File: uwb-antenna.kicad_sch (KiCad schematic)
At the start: 59 parts, among them J1 USB C, J2 Battery, J4 Conn_ST_STDC14, SW1 ~{PB}, SW2 BOOT0, SW4 ~{SR}, U1 STM6600, U2 BQ24074RGT, U3 TPS63001, U5 STM32L432KBUx

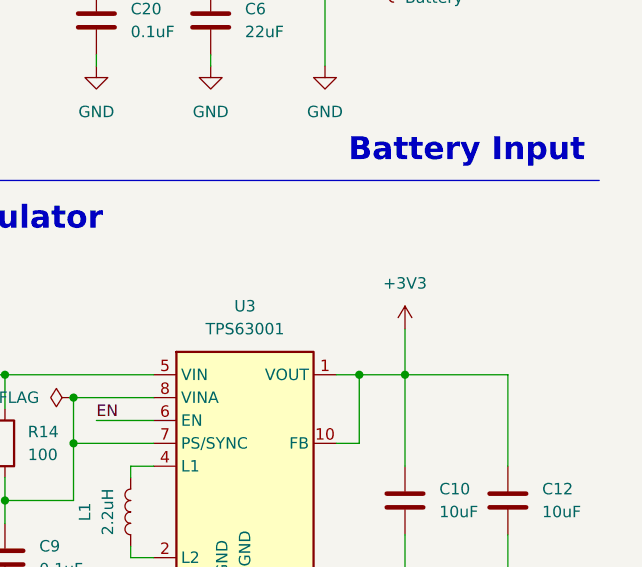
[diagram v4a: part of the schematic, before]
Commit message: add some traces
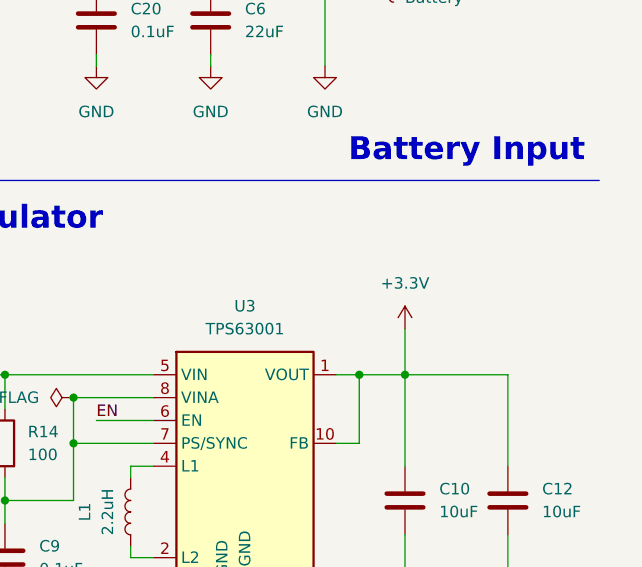
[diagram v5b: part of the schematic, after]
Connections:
- net +3V3 is gone; now on net +3.3V: C10.1, C12.1, U3.1 (VOUT), U3.10 (FB)
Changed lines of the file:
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@@
 	)
 	(symbol
-		(lib_id "power:+3V3")
-		(at 262.89 58.42 0)
-		(unit 1)
-		(exclude_from_sim no)
-		(in_bom yes)
-		(on_board yes)
-		(dnp no)
-		(fields_autoplaced yes)
-		(property "Reference" "#PWR033"
-			(at 262.89 62.23 0)
-			(effects
-				(font
-					(size 1.27 1.27)
-				)
-				(hide yes)
-			)
-		)
-		(property "Value" "+3V3"
-			(at 262.89 53.34 0)
-			(effects
-				(font
-					(size 1.27 1.27)
-				)
-			)
-		)
-		(property "Footprint" ""
-			(at 262.89 58.42 0)
-			(effects
-				(font
-					(size 1.27 1.27)
-				)
-				(hide yes)
-			)
-		)
-		(property "Datasheet" ""
-			(at 262.89 58.42 0)
-			(effects
-				(font
-					(size 1.27 1.27)
-				)
-				(hide yes)
-			)
-		)
-		(property "Description" "Power symbol creates a global label with name \"+3V3\""
-			(at 262.89 58.42 0)
-			(effects
-				(font
-					(size 1.27 1.27)
-				)
-				(hide yes)
-			)
-		)
-		(pin "1"
-		)
-		(instances
-			(project ""
-				(path "/f7e38ffb-df5d-4aea-a3f5-296732509798"
-					(reference "#PWR033")
-					(unit 1)
-				)
-			)
-		)
-	)
-	(symbol
 		(lib_id "Device:C")
 		(at 157.48 139.7 0)
@@
 					(unit 1)
 				)
+			)
+		)
+	)
+	(symbol
+		(lib_id "power:+3.3V")
+		(at 262.89 58.42 0)
+		(unit 1)
+		(exclude_from_sim no)
+		(in_bom yes)
+		(on_board yes)
+		(dnp no)
+		(fields_autoplaced yes)
+		(property "Reference" "#PWR033"
+			(at 262.89 62.23 0)
+			(effects
+				(font
+					(size 1.27 1.27)
+				)
+				(hide yes)
+			)
+		)
+		(property "Value" "+3.3V"
+			(at 262.89 53.34 0)
+			(effects
+				(font
+					(size 1.27 1.27)
+				)
+			)
+		)
+		(property "Footprint" ""
+			(at 262.89 58.42 0)
+			(effects
+				(font
+					(size 1.27 1.27)
+				)
+				(hide yes)
+			)
+		)
+		(property "Datasheet" ""
+			(at 262.89 58.42 0)
+			(effects
+				(font
+					(size 1.27 1.27)
+				)
+				(hide yes)
+			)
+		)
+		(property "Description" "Power symbol creates a global label with name \"+3.3V\""
+			(at 262.89 58.42 0)
+			(effects
+				(font
+					(size 1.27 1.27)
+				)
+				(hide yes)
+			)
+		)
+		(pin "1"
+		)
+		(instances
+			(project "uwb-antenna"
+				(path "/f7e38ffb-df5d-4aea-a3f5-296732509798"
+					(reference "#PWR033")
+					(unit 1)
+				)

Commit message: complete PCB design
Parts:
- removed C16, C17: 0.1uF, Capacitor_SMD:C_0402_1005Metric, symbol Device:C
- removed D1: SP0503BAHT, Package_TO_SOT_SMD:SOT-143, symbol Power_Protection:SP0503BAHT
- removed H2: MH2, MountingHole:MountingHole_3.2mm_M3_Pad, symbol Mechanical:MountingHole
- removed J4: Conn_ST_STDC14, Connector_PinHeader_1.27mm:PinHeader_2x07_P1.27mm_Vertical_SMD, symbol Connector:Conn_ST_STDC14
- removed R3: 0, Resistor_SMD:R_0805_2012Metric, symbol Device:R
- added J3: TC2030-NL, Connector:Tag-Connect_TC2030-IDC-NL_2x03_P1.27mm_Vertical, symbol Connector:Conn_ARM_SWD_TagConnect_TC2030-NL
- added U4: TPD2EUSB30, Package_TO_SOT_SMD:Texas_DRT-3, symbol Power_Protection:TPD2EUSB30
- C10, C11, C12: footprint Capacitor_SMD:C_0201_0603Metric -> Capacitor_SMD:C_0603_1608Metric
- C15: value 0.1uF -> 560nF; LCSC C307331 -> C162174
- R5: footprint Resistor_SMD:R_0805_2012Metric -> Resistor_SMD:R_0402_1005Metric; LCSC C17414 -> C25744
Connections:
- net +3.3V: now also J3.1 (VCC); no longer C15.1
- net D+: now also U4.2 (D-)
- net D-: now also U4.1 (D+)
- net GND: now also J1.S1 (SHIELD), J3.5 (GND), U4.3 (GND)
- net LED_G: now also U5.19 (PA9); no longer U5.18 (PA8)
- net LED_R: now also U5.18 (PA8); no longer U5.19 (PA9)
- net NRST: now also J3.3 (~{RESET})
- net SWCLK: now also J3.4 (SWCLK)
- net SWDIO: now also J3.2 (SWDIO)
- net SWO: now also J3.6 (SWO)
- net UWB_RST: now also U5.2 (PC14); no longer U5.6 (PA0)
- net WAKEUP: now also U5.3 (PC15); no longer U5.7 (PA1)
- net ~{CE}: now also U5.20 (PA10); no longer U5.27 (PB4)
- net at U1.5 (C_SRD): now also C15.1
- no-connect marks 19 -> 13
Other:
- moved on the sheet: C4, H1, U5

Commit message: minors on PCB
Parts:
- C10, C11, C12: LCSC C22399626 -> C48579272
- D3: LCSC C165978 -> C136118
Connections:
- net UWB_RST: now also U5.7 (PA1); no longer U5.2 (PC14)
- net WAKEUP: now also U5.6 (PA0); no longer U5.3 (PC15)
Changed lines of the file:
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@@
 	)
 	(no_connect
-		(at 160.02 36.83)
+		(at 134.62 44.45)
 	)
 	(no_connect
@@
 	)
 	(no_connect
+		(at 134.62 46.99)
+	)
+	(no_connect
 		(at 134.62 167.64)
 	)
@@
 	)
 	(no_connect
-		(at 160.02 34.29)
-	)
-	(no_connect
 		(at 69.85 66.04)
 	)
@@
 	(wire
 		(pts
-			(xy 121.92 46.99) (xy 134.62 46.99)
+			(xy 168.91 34.29) (xy 160.02 34.29)
 		)
 		(stroke
@@
 	(wire
 		(pts
-			(xy 121.92 44.45) (xy 134.62 44.45)
+			(xy 168.91 36.83) (xy 160.02 36.83)
 		)
 		(stroke
@@
 	)
 	(label "UWB_RST"
-		(at 121.92 44.45 0)
+		(at 168.91 36.83 180)
 		(effects
 			(font
 				(size 1.27 1.27)
 			)
-			(justify left bottom)
+			(justify right bottom)
 		)
 	)
@@
 	)
 	(label "WAKEUP"
-		(at 121.92 46.99 0)
+		(at 168.91 34.29 180)
 		(effects
 			(font
 				(size 1.27 1.27)
 			)
-			(justify left bottom)
+			(justify right bottom)
 		)
 	)
@@
 			)
 		)
-		(property "LCSC" "C22399626"
+		(property "LCSC" "C48579272"
 			(at 208.28 77.47 0)
 			(effects
@@
 			)
 		)
-		(property "LCSC" "C165978"
+		(property "LCSC" "C136118"
 			(at 260.35 148.59 0)
 			(effects
@@
 			)
 		)
-		(property "LCSC" "C22399626"
+		(property "LCSC" "C48579272"
 			(at 274.32 77.47 0)
 			(effects
@@
 			)
 		)
-		(property "LCSC" "C22399626"
+		(property "LCSC" "C48579272"
 			(at 262.89 77.47 0)
 			(effects

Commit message: feat: minors in traces and routing
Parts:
- added R18: 20K, Resistor_SMD:R_0402_1005Metric, symbol Device:R
- added R3: 10K, Resistor_SMD:R_0402_1005Metric, symbol Device:R
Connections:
- net BAT: now also R3.1
- net GND: now also R18.2
- net BATT_READ: now reaches U5.9 (PA3)
- net BATT_READ: now also R18.1, R3.2
- no-connect marks 13 -> 12
